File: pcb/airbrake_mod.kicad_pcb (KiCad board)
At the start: 4 copper layers, 65.7 x 107.9 mm, 142 parts, among them J1 XT30PW-M, J2 Same Sky UJ20-C-H-G-SMT-P16-TR, J3 0436500415, J6 CNC_Tech_3220-14-0100-00, Q1 NTR4003N, Q2 NTR4003N, Q3 Si3407DV, Q4 NTR4003N, Q5 Si3407DV, Q6 NTR4003N, SW1 GSPTS0018, SW2 GSPTS0018, SW3 SLW-864574-5A-RA-N-D, SW4 GSPTS0018, SW5 GSPTS0018, SW6 GSPTS0018, SW7 GSPTS0018, U1 STM32H730VBTx, U2 TPS561246DRLR, U3 ZXCT180A4W5, U4 USBLC6-2SC6, U5 W25Q128JVS, U6 LPS22DF, U7 LSM6DSV80X, U8 IIS2MDC, Y1 ECS-160-12-33B2Q-JES-TR3

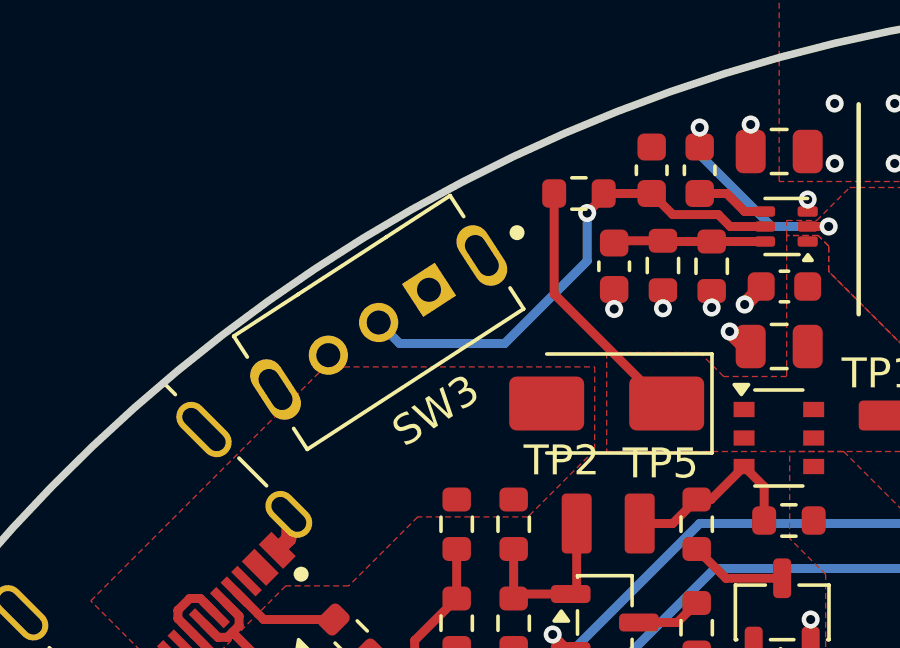
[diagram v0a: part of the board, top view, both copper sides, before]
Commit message: Move switch further from USB C
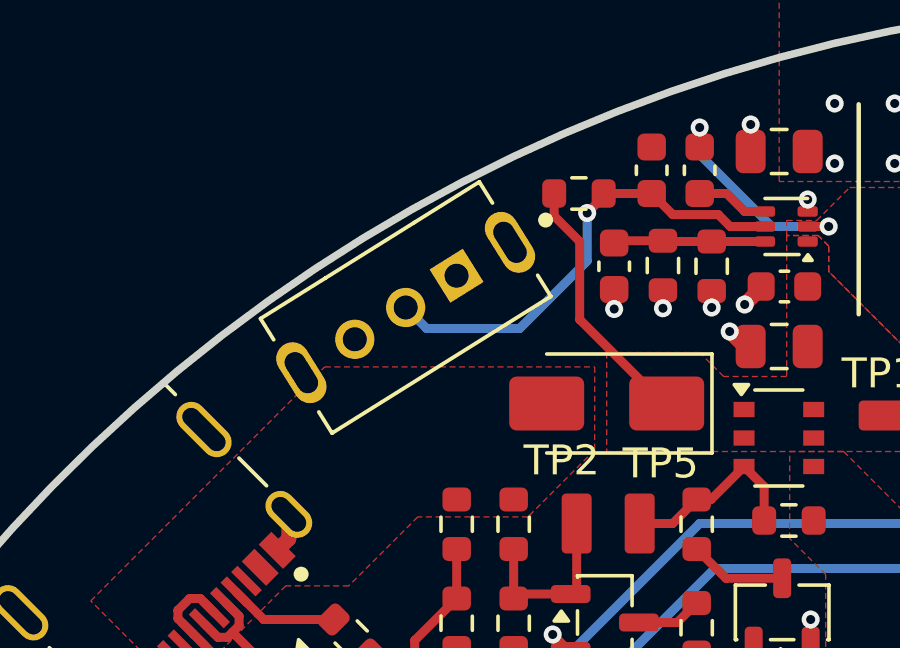
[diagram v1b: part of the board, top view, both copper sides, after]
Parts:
- moved SW3 1.03 mm to (73.2, 56.3), turned to -148 degrees
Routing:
- net Net-(SW3-B): track 16.7 -> 15.6 mm

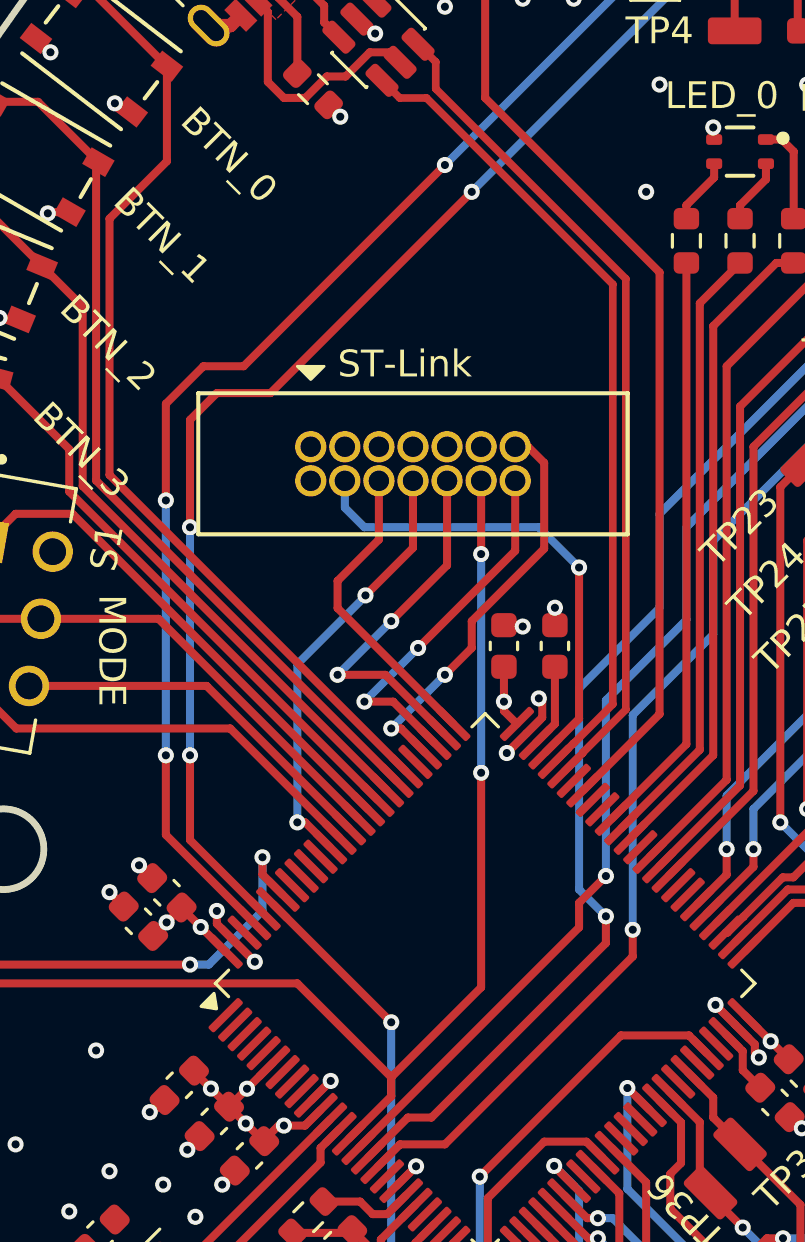
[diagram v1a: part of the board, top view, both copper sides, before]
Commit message: Add ESD protection diode arrays
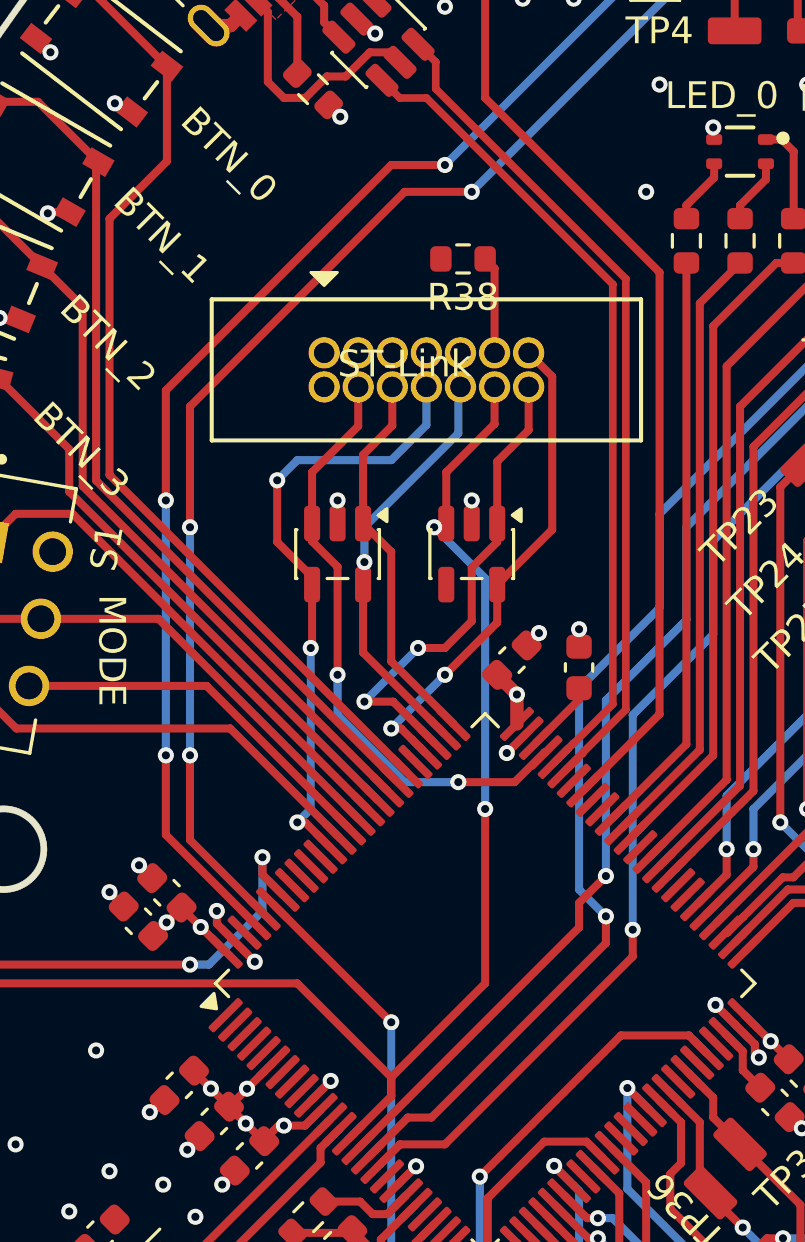
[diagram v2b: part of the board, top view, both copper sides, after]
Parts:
- added D6: ESDA5V3SC5, Package_TO_SOT_SMD:SOT-23-5, F.Cu at (68.0, 89.0)
- added D7: ESDA5V3SC5, Package_TO_SOT_SMD:SOT-23-5, F.Cu at (73.0, 89.0)
- added R38: 100, Resistor_SMD:R_0603_1608Metric, F.Cu at (72.7, 78.0)
- C4, C9: value 14p -> 15p
- moved J6 3.54 mm to (67.5, 81.5)
- moved C2 1.20 mm to (77.0, 93.2)
- moved C14 0.61 mm to (74.5, 93.0), turned to 45 degrees
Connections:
- net /Debug/JCLK renamed /Debug/JCLK/SWCLK
- net /Debug/JTDO renamed /Debug/JTDO/SWO
- net /Debug/JTMS renamed /Debug/JTMS/SWDIO
- J6 pad 11: GND -> Net-(J6-GNDDetect)
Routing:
- net /Debug/JTDO/SWO: track 16.1 -> 23.0 mm, vias 2 -> 3
- net /Debug/~{RESET}: track 54.9 -> 60.4 mm
- net /Debug/JTMS/SWDIO: track 18.1 -> 22.6 mm, vias 1 -> 2
- net /Debug/VCP_TX: track 13.8 -> 18.1 mm
- net Net-(J6-GNDDetect): track 0.00 -> 3.64 mm
- net /Debug/VCP_RX: track 15.2 -> 18.5 mm
- net /Debug/JCLK/SWCLK: track 11.5 -> 14.4 mm
- net /Debug/JTDI: track 13.8 -> 15.7 mm, vias 2 -> 1
- net GND: track 54.1 -> 53.5 mm, vias 101 -> 102

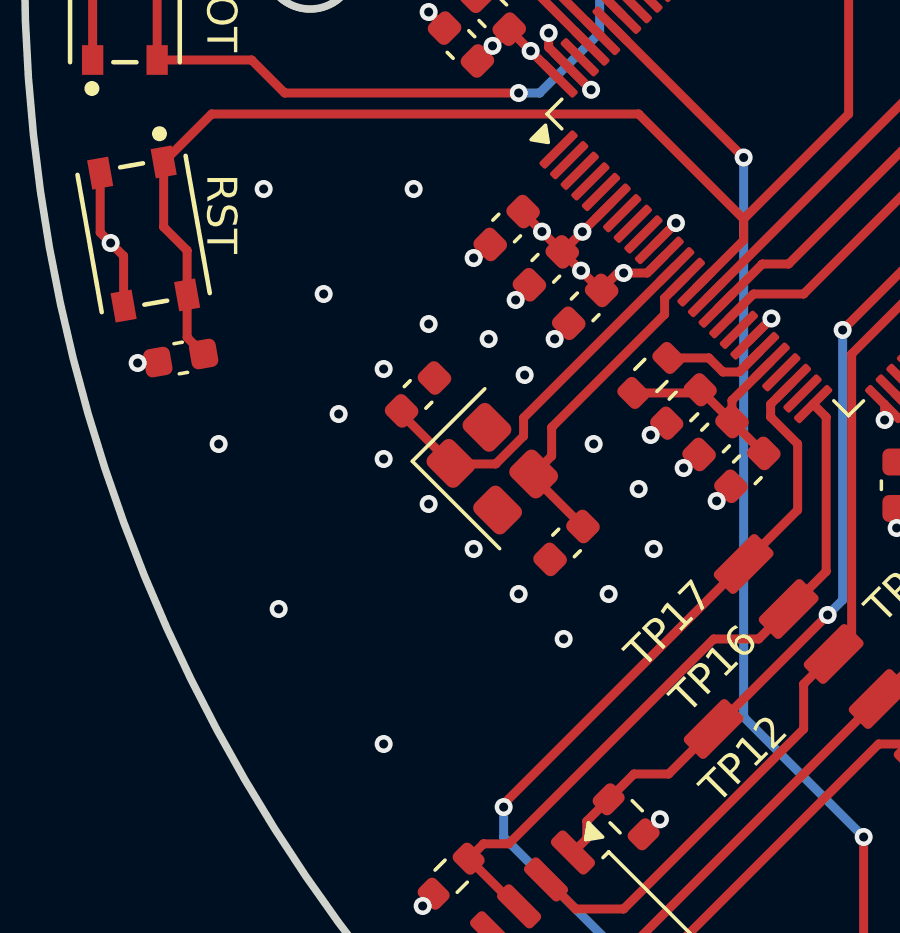
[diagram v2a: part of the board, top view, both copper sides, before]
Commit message: Move crystal closer to MCU
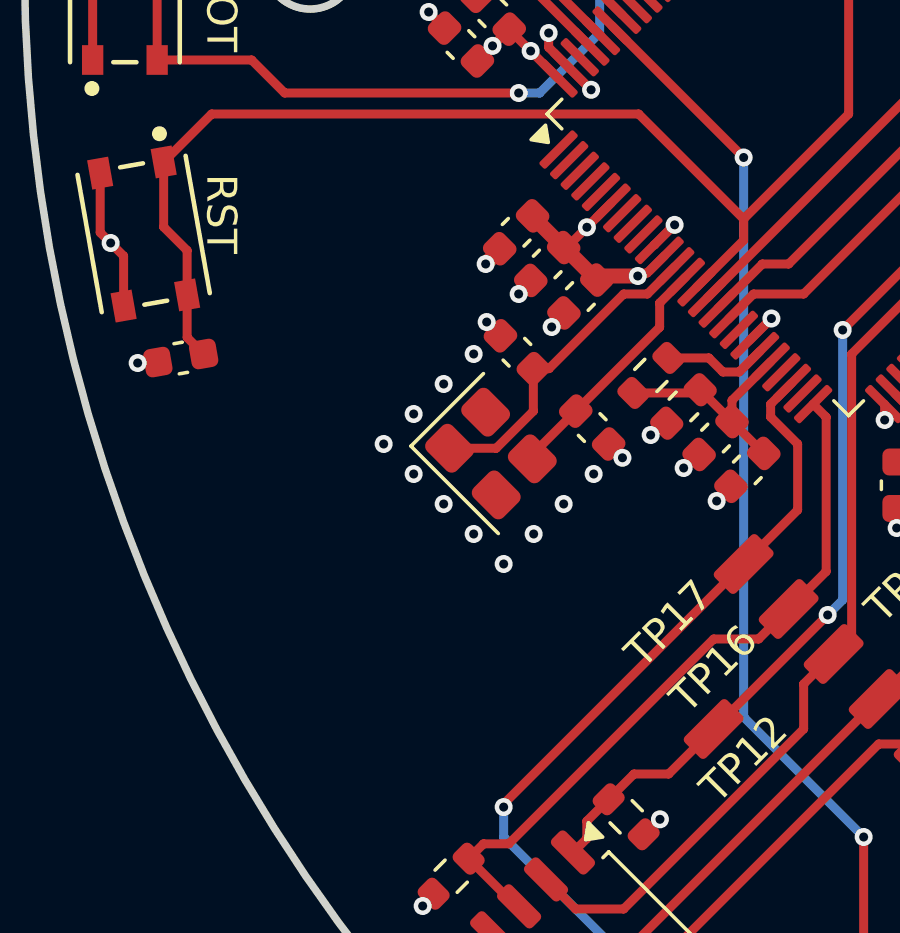
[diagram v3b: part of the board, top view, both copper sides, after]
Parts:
- moved C9 3.94 mm to (65.0, 115.5), turned to -45 degrees
- moved C4 3.58 mm to (62.4, 112.9), turned to 135 degrees
- moved Y1 0.51 mm to (61.6, 116.3)
- moved C7 0.38 mm to (64.6, 111.1)
- moved C12 0.35 mm to (62.4, 108.9)
- moved C15 0.15 mm to (63.5, 110.0)
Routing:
- net /MCU/HSE_OUT: track 11.1 -> 8.19 mm
- net /MCU/HSE_IN: track 13.0 -> 10.9 mm
- net GND: track 53.5 -> 54.5 mm, vias 102 -> 95
- net +3V3: track 68.9 -> 68.1 mm, vias 61 -> 59

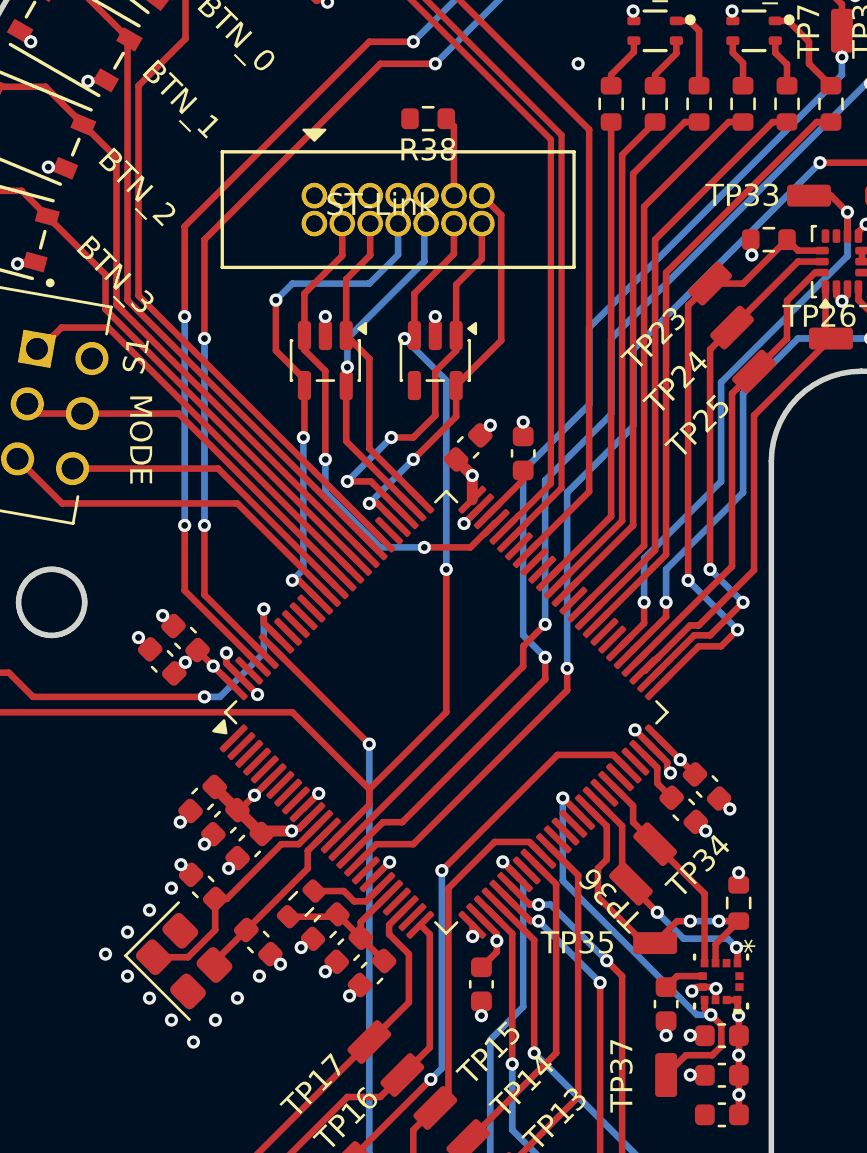
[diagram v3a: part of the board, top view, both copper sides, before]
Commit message: Tweak decoupling capacitor routing
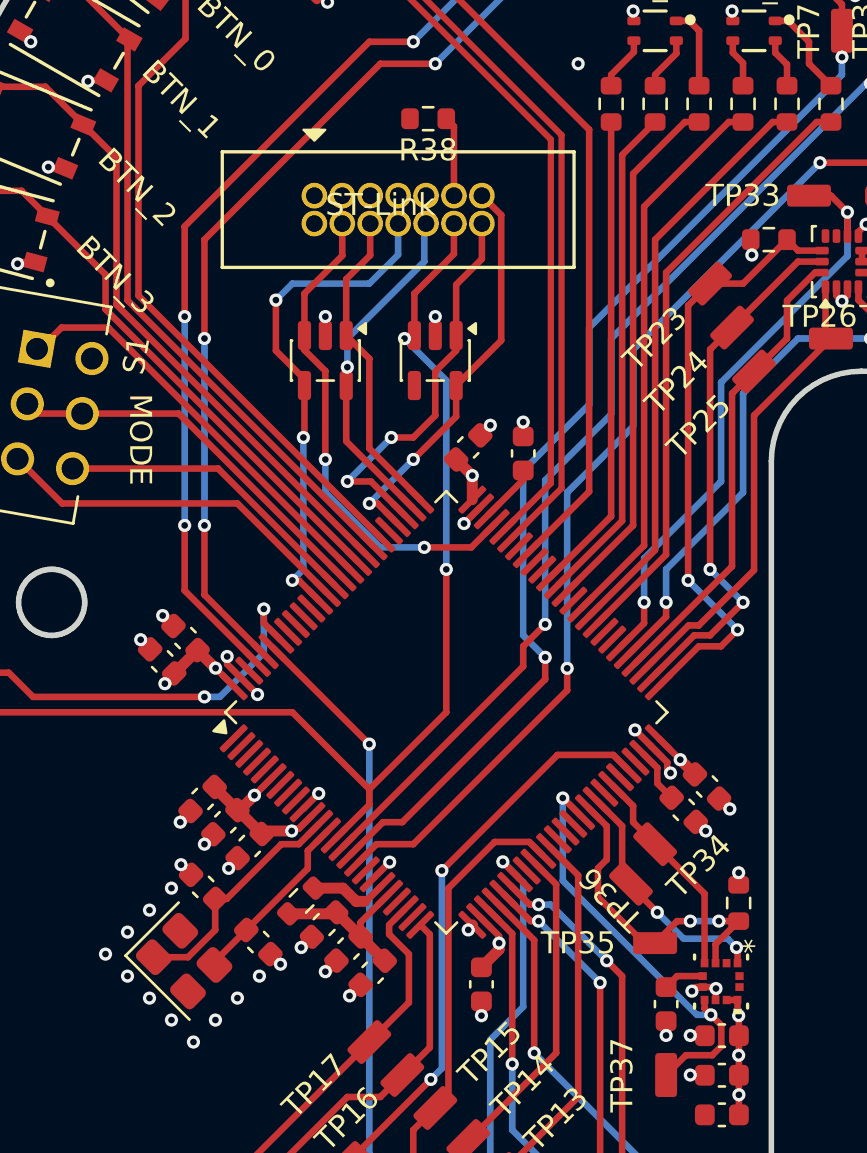
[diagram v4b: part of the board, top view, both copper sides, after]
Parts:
- moved R1 0.13 mm to (66.9, 113.6)
- moved FB1 0.11 mm to (67.9, 114.7)
- moved C6 0.05 mm to (69.1, 115.7)
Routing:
- net +3V3: track 68.1 -> 68.8 mm
- net GND: track 54.5 -> 54.0 mm
